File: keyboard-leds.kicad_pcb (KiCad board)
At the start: 2 copper layers, 89.7 x 51.5 mm, 53 parts, among them J1 USB_C_Receptacle_USB2.0_16P, J2 Conn_01x05, J4 Conn_01x03, J5 USB_C_Receptacle_USB2.0_16P, U1 RP2040, U10 TFT_320x240, U2 W25Q128JVS, U3 XC6206PxxxMR-Regulator_Linear, U5 TUSB320, U6 SN74AHCT1G125DBVR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

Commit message: Cleaned up board a bit
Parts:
- moved Y1 2.00 mm to (155.3, 37.3)
- moved C3 2.00 mm to (151.8, 37.7)
- moved C4 2.00 mm to (154.6, 34.4)
- moved R7 2.00 mm to (156.6, 34.4)
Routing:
- net LCD_BL_PWM: track 95.6 -> 99.3 mm
- net XIN: track 13.2 -> 15.2 mm
- net XOUT: track 24.2 -> 26.2 mm
- net LCD_DC: track 61.4 -> 60.3 mm
- net LCD_RST: track 63.0 -> 61.9 mm
- net LCD_T_CLK: track 58.2 -> 57.3 mm
- net LCD_T_CS: track 59.0 -> 58.2 mm
- net LCD_T_IRQ: track 63.6 -> 62.7 mm
- net LCD_T_DO: track 63.8 -> 62.9 mm
- net LCD_T_DIN: track 60.7 -> 59.8 mm

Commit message: Cleaned up footprints
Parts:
- U10: footprint ILI9341:TFT-320x240 -> ModHob:ILI9341_2.8in_Touch
- moved U10 40.1 mm to (156.3, 39.9)

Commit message: Fixed footprint again, 3d model and routing
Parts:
- moved U2 9.85 mm to (123.0, 41.4)
- moved C5 8.50 mm to (120.6, 47.3)
- moved U10 0.81 mm to (155.8, 39.3)
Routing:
- net Q_SEL: track 62.0 -> 38.5 mm
- net Q_IO1: track 23.4 -> 13.1 mm
- net Q_IO0: track 12.9 -> 22.4 mm
- net Q_IO2: track 18.1 -> 11.4 mm
- net +3V3: track 211.5 -> 216.0 mm
- net Q_IO3: track 17.5 -> 21.8 mm
- net Net-(U1-USB_DM): track 47.0 -> 50.9 mm
- net Net-(U1-USB_DP): track 47.6 -> 51.2 mm
- net GND: vias 20 -> 18

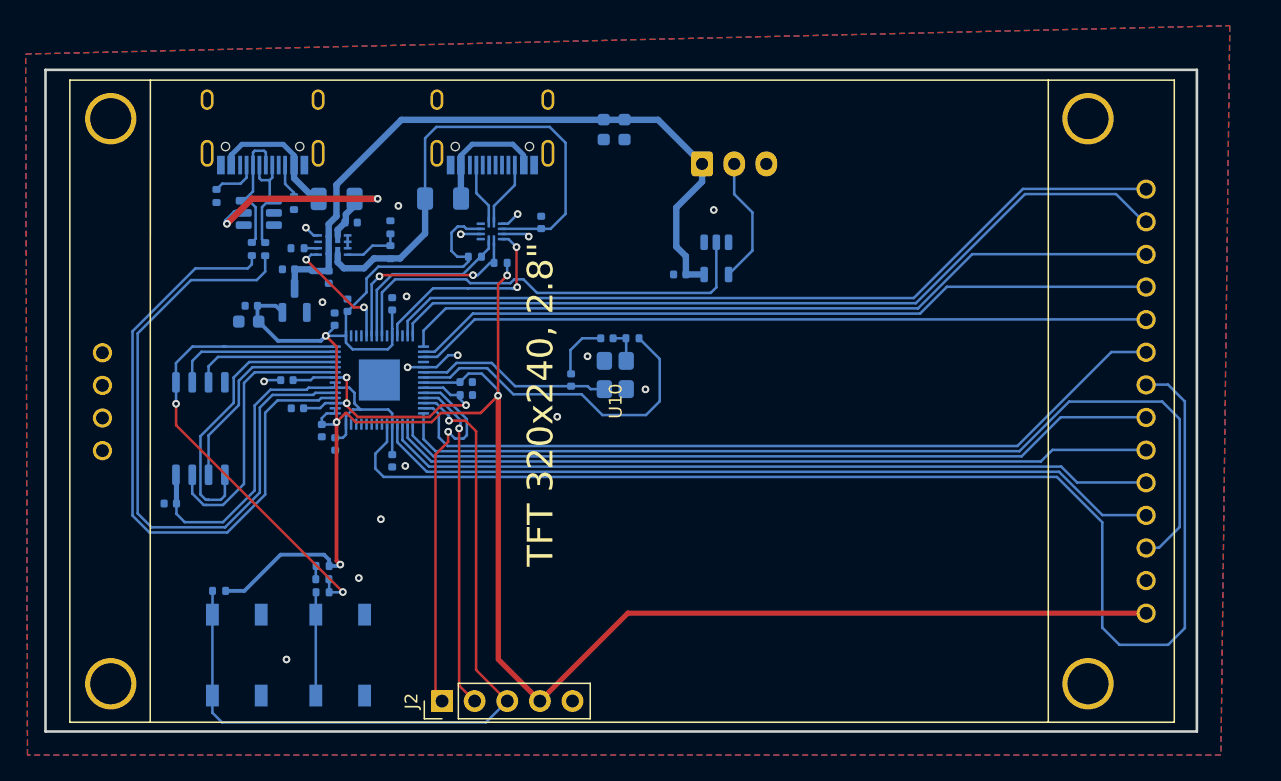
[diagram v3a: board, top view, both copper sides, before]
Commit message: Wired up SD Card, joined SPI devices
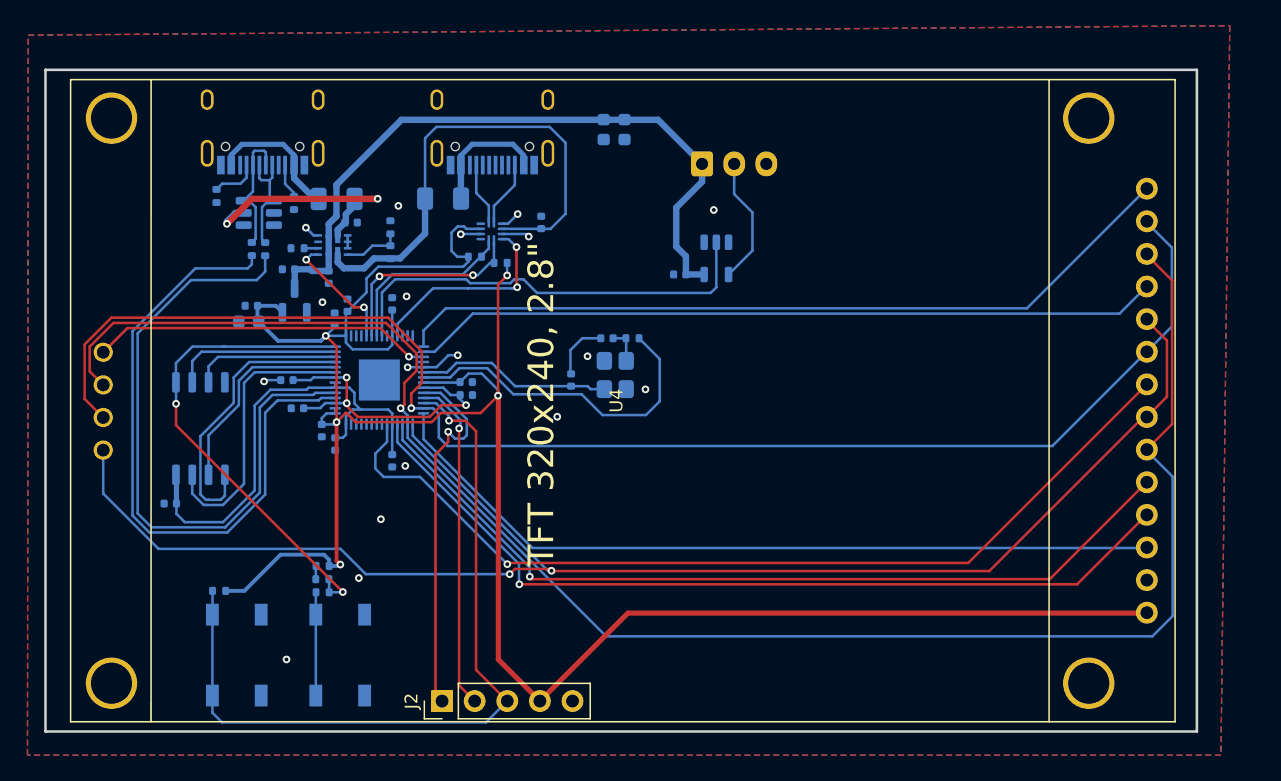
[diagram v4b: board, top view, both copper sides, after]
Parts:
- removed U10: TFT_320x240, ModHob:ILI9341_2.8in_Touch
- added U4: TFT_320x240, ModHob:ILI9341_2.8in_Touch, F.Cu at (155.9, 39.3)
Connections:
- U1 pad 13: LCD_T_IRQ -> unconnected-(U1-GPIO10-Pad13)
- U1 pad 14: LCD_T_DO -> unconnected-(U1-GPIO11-Pad14)
- U1 pad 15: LCD_T_DIN -> LCD_T_IRQ
- U1 pad 17: LCD_T_CLK -> LCD_SD_CS
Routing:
- net LCD_MOSI: track 59.5 -> 135.2 mm, vias 0 -> 1
- net LCD_T_DO: track 62.9 -> 0.00 mm
- net LCD_T_DIN: track 59.8 -> 0.00 mm
- net LCD_SCK: track 59.7 -> 117.4 mm, vias 0 -> 2
- net LCD_T_CLK: track 57.3 -> 0.00 mm
- net LCD_MISO: track 61.4 -> 113.6 mm, vias 0 -> 1
- net LCD_SD_CS: track 0.00 -> 26.6 mm, vias 0 -> 1
- net LCD_BL_PWM: track 99.3 -> 72.7 mm, vias 0 -> 1
- net LCD_CS: track 75.3 -> 61.8 mm
- net LCD_DC: track 60.3 -> 67.2 mm, vias 0 -> 1
- net LCD_RST: track 61.9 -> 67.4 mm, vias 0 -> 1
- net LCD_T_IRQ: track 62.7 -> 62.1 mm

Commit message: Added logo and text to PCB
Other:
- board text added: "Project Keylight: Mk. I MIDI Based LED Controller"

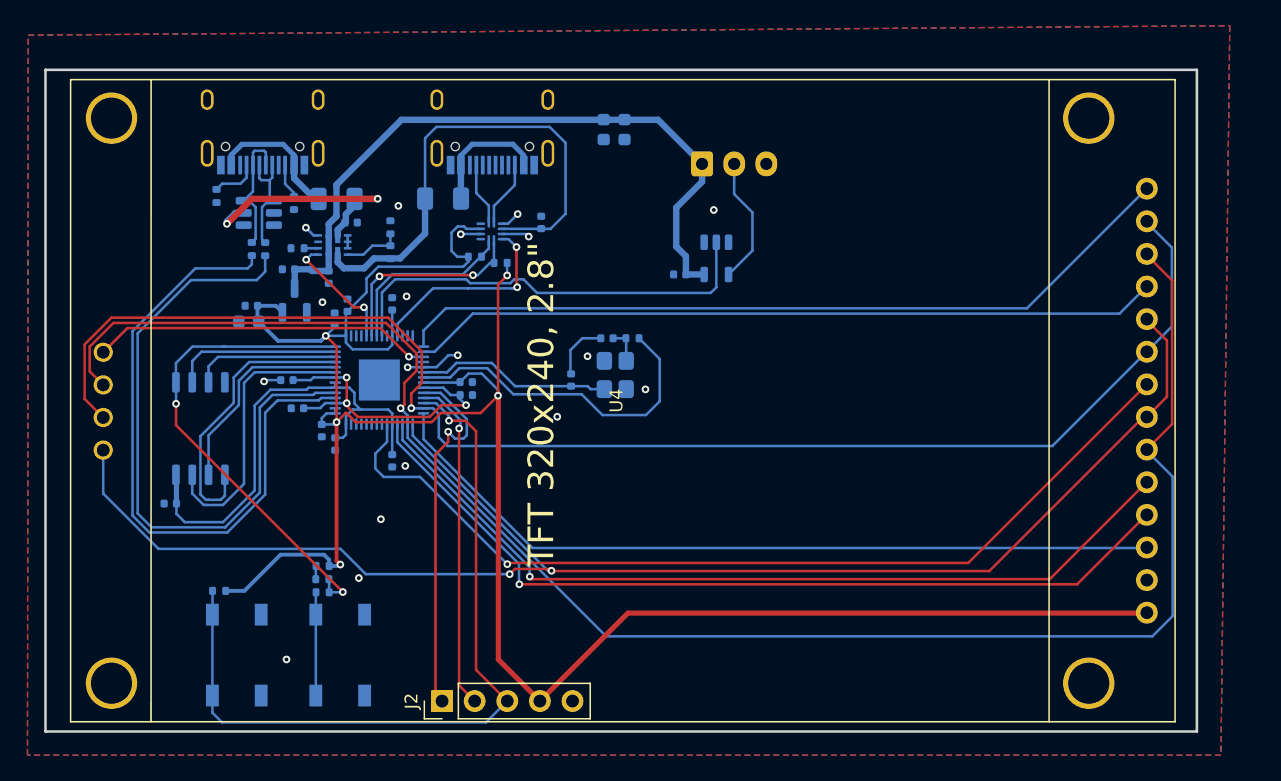
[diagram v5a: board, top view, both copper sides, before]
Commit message: Moved led output to other side for better cable management
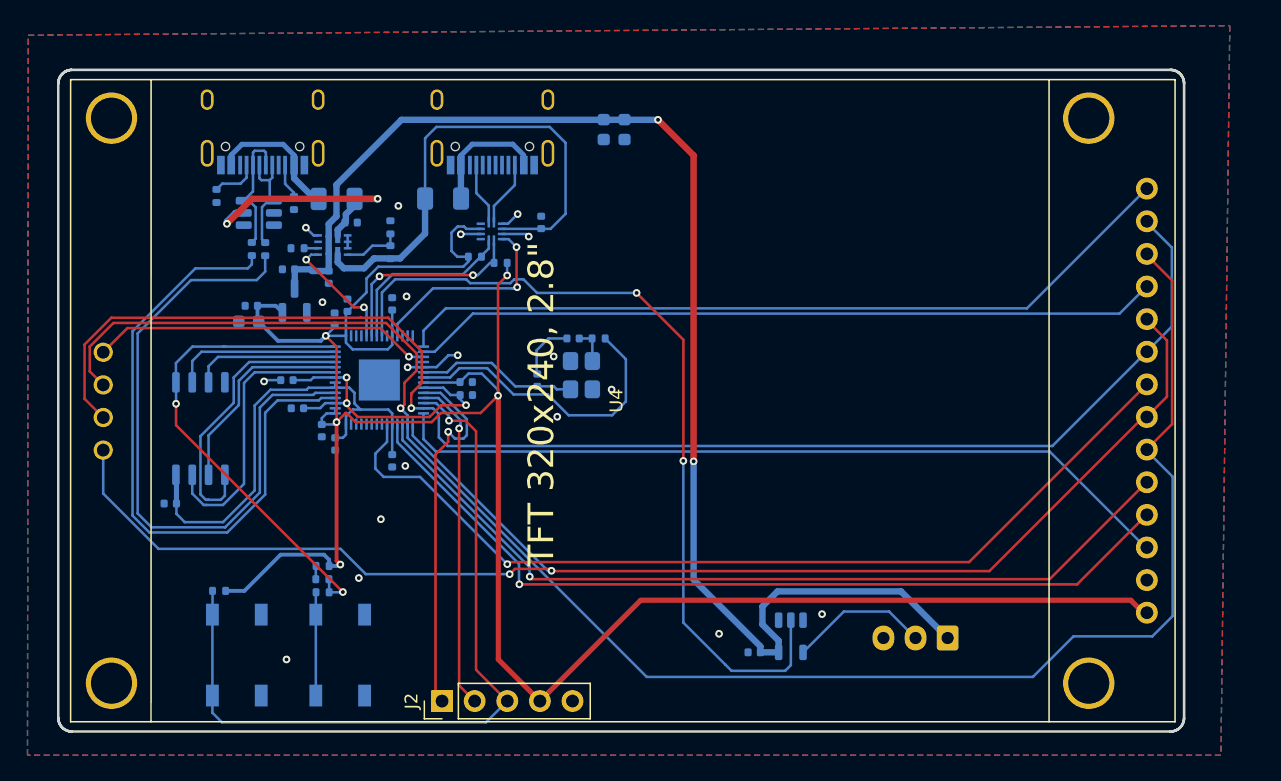
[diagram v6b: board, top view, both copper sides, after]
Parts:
- moved J4 41.6 mm to (181.2, 57.8), turned to 180 degrees
- moved C112 30.0 mm to (166.1, 58.9)
- moved U6 30.0 mm to (168.9, 57.6)
- moved C3 2.64 mm to (149.2, 37.7)
- moved R7 2.64 mm to (154.0, 34.4)
- moved Y1 2.64 mm to (152.6, 37.3)
- moved C4 2.64 mm to (152.0, 34.4)
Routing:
- net +5V: track 54.3 -> 105.0 mm, vias 0 -> 2
- net RGB3.3: track 34.2 -> 65.1 mm, vias 0 -> 2
- net XIN: track 15.2 -> 12.6 mm
- net XOUT: track 26.2 -> 23.6 mm
- net LCD_MOSI: track 135.2 -> 137.9 mm
- net RGB5v: track 9.97 -> 10.9 mm
- net +3V3: track 216.0 -> 216.8 mm
- net GND: vias 18 -> 19
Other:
- board size 89.7 x 51.5 mm -> 87.7 x 51.5 mm
- board text added: "+3V3"
- board text added: "GND"
- board text added: "RESET"
- board text added: "SWC"
- board text added: "SWD"
